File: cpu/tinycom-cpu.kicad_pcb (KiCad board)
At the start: 4 copper layers, 39.9 x 41.4 mm, 4 parts, among them P1 CONN_02X08, P2 CONN_02X08, U1 OLIMEX_IC_A13, U2 H5TQG63BFR/FBGA96

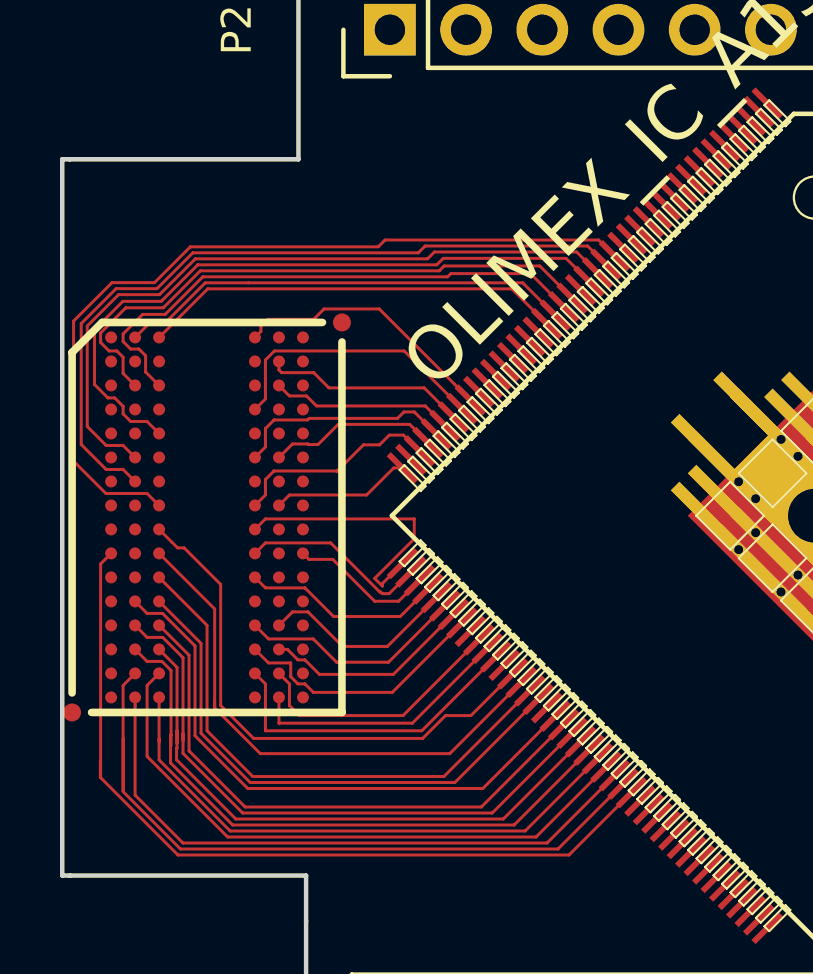
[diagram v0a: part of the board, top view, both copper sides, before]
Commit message: add missing ddr connecitons
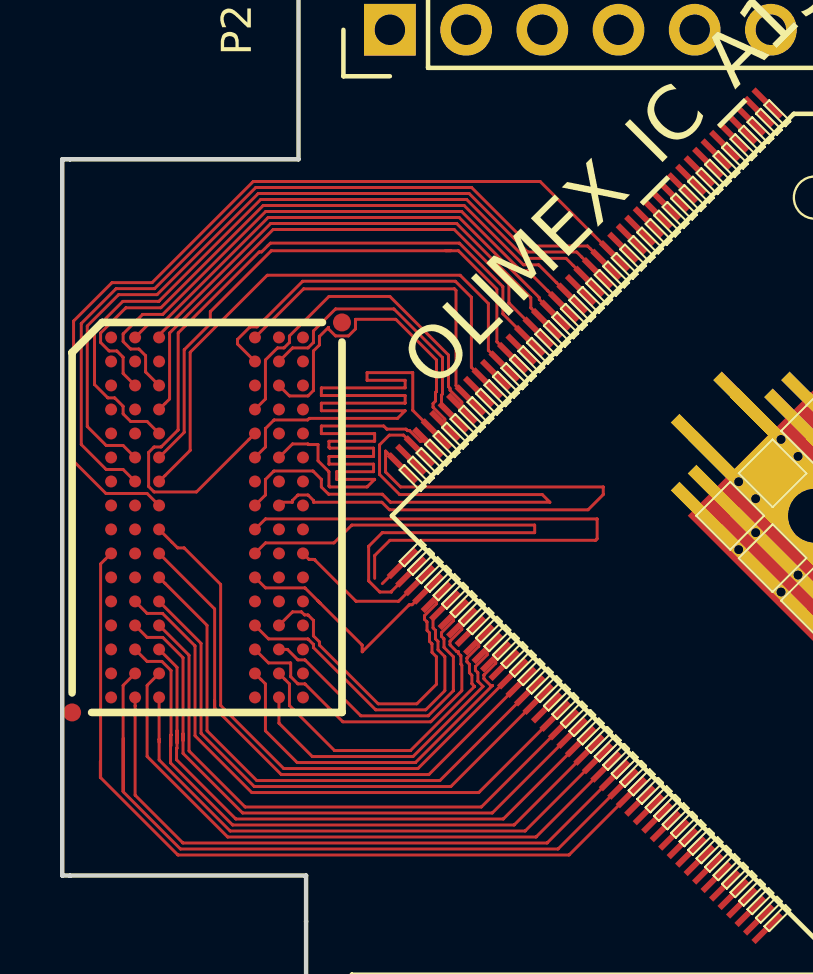
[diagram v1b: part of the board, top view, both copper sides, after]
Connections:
- net DQS1 renamed DDR_DQS1_P
- U2 pad B7: DQS1N -> DDR_DQS1_N
- U2 pad D3: DQM1 -> DDR_DQM1
- U2 pad E7: DQM0 -> DDR_DQM0
- U2 pad F3: DQS0 -> DDR_DQS0_P
- U2 pad G3: DQS0N -> DDR_DQS0_N
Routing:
- net DDR_DQM0: track 0.00 -> 24.9 mm
- net DDR_DQS0_P: track 0.00 -> 19.2 mm
- net DDR_DQS0_N: track 0.00 -> 18.4 mm
- net DDR_DQM1: track 0.00 -> 18.2 mm
- net DDR_D1: track 7.34 -> 23.6 mm
- net DDR_D5: track 4.64 -> 20.7 mm
- net DDR_D3: track 5.69 -> 20.5 mm
- net DDR_D7: track 6.99 -> 19.9 mm
- net DDR_DQS1_N: track 0.00 -> 12.9 mm
- net DDR_CK_N: track 6.34 -> 18.7 mm
- net DDR_CK_P: track 9.37 -> 21.6 mm
- net DDR_D10: track 6.08 -> 10.8 mm
- net DDR_BA1: track 6.59 -> 10.6 mm
- net DDR_A12: track 7.62 -> 11.0 mm
- net DDR_A4: track 6.99 -> 9.95 mm
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
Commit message: add routes
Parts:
- added C1: C_Small, Capacitors_SMD:C_0603, F.Cu at (112.8, 121.2)
- added C2: C_Small, Capacitors_SMD:C_0603, F.Cu at (116.3, 118.4)
- added R1: R, Resistors_SMD:R_0603, F.Cu at (88.9, 122.7)
- added R2: R, Resistors_SMD:R_0603, F.Cu at (88.9, 124.5)
- added R3: R, Resistors_SMD:R_0603, F.Cu at (80.8, 100.3)
- added Y1: Crystal, Crystals:crystal_FA238-TSX3225, F.Cu at (115.8, 120.9)
- moved P1 18.5 mm to (107.7, 127.3), turned to 270 degrees
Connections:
- P1 pad 1: Net-(P1-Pad1) -> SDC0_D1
- P1 pad 10: Net-(P1-Pad10) -> VCC_14
- P1 pad 11: Net-(P1-Pad11) -> SDC0_D2
- P1 pad 12: Net-(P1-Pad12) -> VCC_15
- P1 pad 13: Net-(P1-Pad13) -> UART1_TX
- P1 pad 14: Net-(P1-Pad14) -> VCC_30
- P1 pad 15: Net-(P1-Pad15) -> UART1_RX
- P1 pad 16: Net-(P1-Pad16) -> VCC_33
- P1 pad 2: Net-(P1-Pad2) -> UDM0
- P1 pad 3: Net-(P1-Pad3) -> SDC0_D0
- P1 pad 4: Net-(P1-Pad4) -> UDP0
- P1 pad 5: Net-(P1-Pad5) -> SDC0_CLK
- P1 pad 6: Net-(P1-Pad6) -> UDM1
- P1 pad 7: Net-(P1-Pad7) -> SDC0_CMD
- P1 pad 8: Net-(P1-Pad8) -> UDP1
- P1 pad 9: Net-(P1-Pad9) -> SDC0_D3
- P2 pad 1: Net-(P2-Pad1) -> CSI_CLK
- P2 pad 10: Net-(P2-Pad10) -> GND
- P2 pad 11: Net-(P2-Pad11) -> CSI_D1
- P2 pad 12: Net-(P2-Pad12) -> GND
- P2 pad 13: Net-(P2-Pad13) -> CSI_D2
- P2 pad 14: Net-(P2-Pad14) -> GND
- P2 pad 15: Net-(P2-Pad15) -> CSI_D3
- P2 pad 16: Net-(P2-Pad16) -> GND
- P2 pad 2: Net-(P2-Pad2) -> CSI_D4
- P2 pad 3: Net-(P2-Pad3) -> CSI_MCLK
- P2 pad 4: Net-(P2-Pad4) -> CSI_D5
- P2 pad 5: Net-(P2-Pad5) -> CSI_HSYNC
- P2 pad 6: Net-(P2-Pad6) -> CSI_D6
- P2 pad 7: Net-(P2-Pad7) -> CSI_VSYNC
- P2 pad 8: Net-(P2-Pad8) -> CSI_D7
- P2 pad 9: Net-(P2-Pad9) -> CSI_D0
- U1 pad 100: Net-(U1-Pad100) -> VCC_33
- U1 pad 107: Net-(U1-Pad107) -> SDC0_D1
- U1 pad 108: Net-(U1-Pad108) -> SDC0_D0
- U1 pad 109: Net-(U1-Pad109) -> VCC_14
- U1 pad 11: Net-(U1-Pad11) -> VCC_14
- U1 pad 110: Net-(U1-Pad110) -> SDC0_CLK
- U1 pad 111: Net-(U1-Pad111) -> SDC0_CMD
- U1 pad 112: Net-(U1-Pad112) -> SDC0_D3
- U1 pad 113: Net-(U1-Pad113) -> SDC0_D2
- U1 pad 114: Net-(U1-Pad114) -> CSI_CLK
- U1 pad 115: Net-(U1-Pad115) -> CSI_MCLK
- U1 pad 116: Net-(U1-Pad116) -> CSI_HSYNC
- U1 pad 117: Net-(U1-Pad117) -> CSI_VSYNC
- U1 pad 118: Net-(U1-Pad118) -> CSI_D0
- U1 pad 119: Net-(U1-Pad119) -> CSI_D1
- U1 pad 120: Net-(U1-Pad120) -> CSI_D2
- U1 pad 121: Net-(U1-Pad121) -> CSI_D3
- U1 pad 122: Net-(U1-Pad122) -> CSI_D4
- U1 pad 123: Net-(U1-Pad123) -> CSI_D5
- U1 pad 124: Net-(U1-Pad124) -> CSI_D6
- U1 pad 125: Net-(U1-Pad125) -> CSI_D7
- U1 pad 142: Net-(U1-Pad142) -> VCC_33
- U1 pad 149: Net-(U1-Pad149) -> VCC_14
- U1 pad 151: Net-(U1-Pad151) -> UART1_RX
- U1 pad 152: Net-(U1-Pad152) -> UART1_TX
- U1 pad 156: Net-(U1-Pad156) -> VCC_14
- U1 pad 159: Net-(U1-Pad159) -> GND
- U1 pad 16: Net-(U1-Pad16) -> VCC_14
- U1 pad 163: Net-(U1-Pad163) -> VCC_33
- U1 pad 164: Net-(U1-Pad164) -> VCC_14
- U1 pad 169: Net-(U1-Pad169) -> VCC_14
- U1 pad 173: Net-(U1-Pad173) -> VCC_14
- U1 pad 23: Net-(U1-Pad23) -> VCC_15
- U1 pad 30: Net-(U1-Pad30) -> VCC_15
- U1 pad 35: Net-(U1-Pad35) -> VCC_14
- U1 pad 4: Net-(U1-Pad4) -> VCC_14
- U1 pad 43: Net-(U1-Pad43) -> VCC_15
- U1 pad 5: Net-(U1-Pad5) -> VCC_33
- U1 pad 53: Net-(U1-Pad53) -> VCC_15
- U1 pad 62: Net-(U1-Pad62) -> VCC_15
- U1 pad 73: Net-(U1-Pad73) -> VCC_14
- U1 pad 76: Net-(U1-Pad76) -> VCC_33
- U1 pad 80: Net-(U1-Pad80) -> VCC_33
- U1 pad 81: Net-(U1-Pad81) -> VCC_30
- U1 pad 82: Net-(U1-Pad82) -> VCC_33
- U1 pad 83: Net-(U1-Pad83) -> VCC_33
- U1 pad 9: Net-(U1-Pad9) -> VCC_14
- U1 pad 93: Net-(U1-Pad93) -> UDM0
- U1 pad 94: Net-(U1-Pad94) -> UDP0
- U1 pad 95: Net-(U1-Pad95) -> UDM1
- U1 pad 96: Net-(U1-Pad96) -> UDP1
- U1 pad 97: Net-(U1-Pad97) -> VCC_33
- U1 pad 98: Net-(U1-Pad98) -> VCC_14
- U1 pad GND_: Net-(U1-PadGND_) -> Net-(U1-Pad79)
- U2 pad A1: Net-(U2-PadA1) -> VCC_15
- U2 pad A8: Net-(U2-PadA8) -> VCC_15
- U2 pad A9: Net-(U2-PadA9) -> GND
- U2 pad B1: Net-(U2-PadB1) -> GND
- U2 pad B2: Net-(U2-PadB2) -> VCC_15
- U2 pad B3: Net-(U2-PadB3) -> GND
- U2 pad B9: Net-(U2-PadB9) -> GND
- U2 pad C1: Net-(U2-PadC1) -> VCC_15
- U2 pad C9: Net-(U2-PadC9) -> VCC_15
- U2 pad D1: Net-(U2-PadD1) -> GND
- U2 pad D2: Net-(U2-PadD2) -> VCC_15
- U2 pad D8: Net-(U2-PadD8) -> GND
- U2 pad D9: Net-(U2-PadD9) -> VCC_15
- U2 pad E1: Net-(U2-PadE1) -> GND
- U2 pad E2: Net-(U2-PadE2) -> GND
- U2 pad E8: Net-(U2-PadE8) -> GND
- U2 pad E9: Net-(U2-PadE9) -> VCC_15
- U2 pad F1: Net-(U2-PadF1) -> VCC_15
- U2 pad F9: Net-(U2-PadF9) -> GND
- U2 pad G1: Net-(U2-PadG1) -> GND
- U2 pad G7: Net-(U2-PadG7) -> VCC_15
- U2 pad G8: Net-(U2-PadG8) -> GND
- U2 pad G9: Net-(U2-PadG9) -> GND
- U2 pad H1: Net-(U2-PadH1) -> Net-(R1-Pad2)
- U2 pad H2: Net-(U2-PadH2) -> VCC_15
- U2 pad H9: Net-(U2-PadH9) -> VCC_15
- U2 pad J2: Net-(U2-PadJ2) -> GND
- U2 pad J8: Net-(U2-PadJ8) -> GND
- U2 pad K2: Net-(U2-PadK2) -> VCC_15
- U2 pad K8: Net-(U2-PadK8) -> VCC_15
- U2 pad L2: Net-(U2-PadL2) -> GND
- U2 pad M1: Net-(U2-PadM1) -> GND
- U2 pad M8: Net-(U2-PadM8) -> Net-(R1-Pad2)
- U2 pad M9: Net-(U2-PadM9) -> GND
- U2 pad N1: Net-(U2-PadN1) -> VCC_15
- U2 pad N9: Net-(U2-PadN9) -> VCC_15
- U2 pad P1: Net-(U2-PadP1) -> GND
- U2 pad P9: Net-(U2-PadP9) -> GND
- U2 pad R1: Net-(U2-PadR1) -> VCC_15
- U2 pad R9: Net-(U2-PadR9) -> VCC_15
- U2 pad T1: Net-(U2-PadT1) -> GND
- U2 pad T9: Net-(U2-PadT9) -> GND
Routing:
- net CSI_D4: track 0.00 -> 37.3 mm, vias 0 -> 1
- net UART1_RX: track 0.00 -> 35.6 mm, vias 0 -> 1
- net CSI_CLK: track 0.00 -> 35.4 mm, vias 0 -> 1
- net CSI_D5: track 0.00 -> 34.5 mm, vias 0 -> 1
- net UART1_TX: track 0.00 -> 34.2 mm, vias 0 -> 1
- net CSI_MCLK: track 0.00 -> 32.6 mm, vias 0 -> 1
- net CSI_D6: track 0.00 -> 31.7 mm, vias 0 -> 1
- net CSI_HSYNC: track 0.00 -> 30.3 mm, vias 0 -> 1
- net CSI_D7: track 0.00 -> 30.1 mm, vias 0 -> 1
- net CSI_VSYNC: track 0.00 -> 28.7 mm, vias 0 -> 1
- net CSI_D0: track 0.00 -> 27.5 mm, vias 0 -> 1
- net CSI_D1: track 0.00 -> 27.1 mm, vias 0 -> 1
- net CSI_D2: track 0.00 -> 25.1 mm, vias 0 -> 1
- net CSI_D3: track 0.00 -> 23.8 mm, vias 0 -> 1
- net SDC0_D2: track 0.00 -> 22.0 mm, vias 0 -> 1
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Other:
- net class Default: clearance 0.1 -> 0.15
- net class ddr_address: clearance 0.1 -> 0.15
- net class ddr_byte_0: clearance 0.1 -> 0.15
- net class ddr_byte_1: clearance 0.1 -> 0.15
- net class ddr_clock: clearance 0.1 -> 0.15
- net class ddr_control: clearance 0.1 -> 0.15
- rule trace_clearance: 0.1 -> 0.15

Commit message: add routes
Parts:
- turned R1 to 180 degrees
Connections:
- P2 pad 10: GND -> MICIN1
- U1 pad 84: Net-(U1-Pad84) -> MICIN1
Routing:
- net VCC_15: track 0.00 -> 62.7 mm, vias 0 -> 19
- net MICIN1: track 0.00 -> 58.6 mm, vias 0 -> 1
- net VCC_33: track 0.00 -> 28.3 mm, vias 0 -> 8
- net VCC_14: track 0.00 -> 15.9 mm, vias 0 -> 13
- net GND: track 0.00 -> 7.14 mm, vias 0 -> 10
- net SDC0_D1: track 17.4 -> 11.0 mm
- net SDC0_D0: track 15.7 -> 12.9 mm
- net VCC_30: track 0.00 -> 1.63 mm, vias 0 -> 1
- net SDC0_CLK: track 15.9 -> 14.9 mm
- net CSI_D4: track 37.3 -> 36.6 mm
- net CSI_CLK: track 35.4 -> 34.7 mm
- net CSI_MCLK: track 32.6 -> 31.9 mm
- net UART1_RX: track 35.6 -> 36.2 mm
- net DDR_D5: track 5.29 -> 4.79 mm
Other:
- net class vcc_15 added: clearance 0.15, trace_width 0.1, via_dia 0.2, via_drill 0.1
- net class vcc_33 added: clearance 0.15, trace_width 0.15, via_dia 0.2, via_drill 0.1

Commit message: full ddr route
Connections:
- U2 pad J9: Net-(U2-PadJ9) -> GND
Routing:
- net GND: track 7.14 -> 17.0 mm, vias 10 -> 18
- net DDR_DQS1_N: track 10.9 -> 6.17 mm
- net DDR_D12: track 8.85 -> 4.32 mm
- net DDR_D7: track 7.14 -> 9.54 mm
- net DDR_D1: track 7.16 -> 8.94 mm
- net DDR_D14: track 6.96 -> 8.57 mm
- net DDR_D8: track 10.1 -> 8.51 mm
- net DDR_CK_P: track 6.78 -> 5.72 mm
- net DDR_D2: track 24.0 -> 23.1 mm
- net DDR_D11: track 19.8 -> 19.0 mm
- net DDR_D10: track 6.08 -> 6.81 mm
- net DDR_D0: track 23.2 -> 22.5 mm
- net VCC_15: track 62.7 -> 63.0 mm, vias 19 -> 21

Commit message: fix ddr routing
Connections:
- U1 pad 33: DDR_QDS1_P -> DDR_DQS1_P
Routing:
- net DDR_DQS1_P: track 0.00 -> 13.3 mm
- net DDR_DQS1_N: track 6.17 -> 11.7 mm
- net DDR_D12: track 4.32 -> 9.63 mm
- net DDR_D2: track 23.1 -> 26.8 mm
- net DDR_D11: track 19.0 -> 22.6 mm
- net DDR_D8: track 8.51 -> 12.0 mm
- net DDR_D0: track 22.5 -> 25.4 mm
- net DDR_D4: track 28.3 -> 30.5 mm
- net DDR_D6: track 25.7 -> 27.9 mm
- net DDR_D14: track 8.57 -> 7.14 mm
- net GND: track 17.0 -> 18.2 mm, vias 18 -> 20
- net DDR_D13: track 15.7 -> 16.8 mm
- net DDR_DQM0: track 23.2 -> 24.2 mm
- net DDR_DQS0_P: track 16.7 -> 17.6 mm
- net DDR_D9: track 18.7 -> 19.6 mm
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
